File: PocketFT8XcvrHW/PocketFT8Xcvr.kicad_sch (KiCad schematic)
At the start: 56 parts, among them J1 HX8357D SPI, J2 22-23-2021, J3 GPS, J5 HX8357D 8-BIT, Q1 2N3904, Q2 2N3906, Q3 2N7000, Q4 2N7000, U1 MCP3422A1T-E/SN, U2 Si4735-D60-GU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

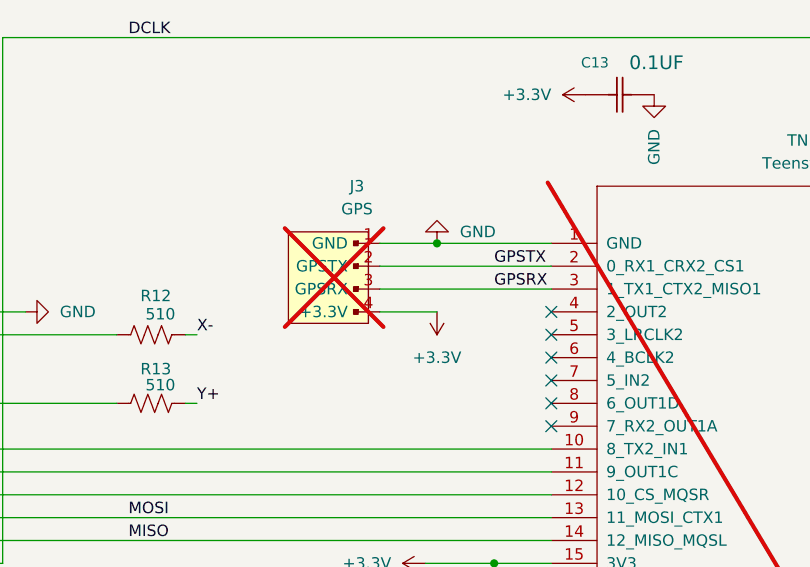
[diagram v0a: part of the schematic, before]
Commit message: Revise GPS Connector
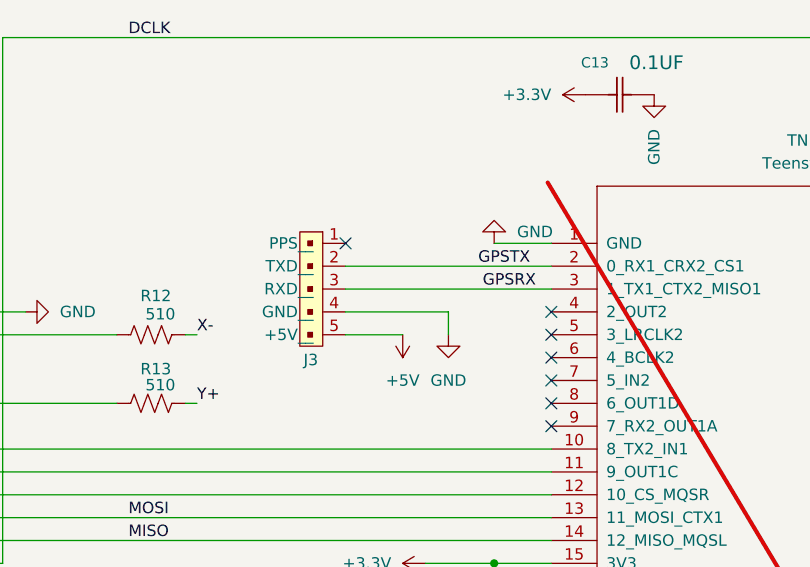
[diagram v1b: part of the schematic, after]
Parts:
- removed J3: GPS, digikey-footprints:PinHeader_1x4_P2.54mm_Drill1.02mm, symbol dk_Rectangular-Connectors-Headers-Male-Pins:0022232041
- added J3: B5B-XH-A_LF__SN_, digikey-footprints:PinHeader_1x5_P2.5mm_Drill1.1mm, symbol dk_Rectangular-Connectors-Headers-Male-Pins:B5B-XH-A_LF__SN_
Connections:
- net +5V: now also J3.5 (+5V__)
- net GND: now also J3.4 (GND__)
- net GPSRX: now also J3.3 (RXD__)
- net GPSTX: now also J3.2 (TXD__)
- no-connect marks 83 -> 84

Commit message: DRC Cleanup
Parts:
- added C18: 0.1UF, Capacitor_SMD:C_0603_1608Metric, symbol Kemet2024-08-02_22-05-35:C0603C104K4RACTU
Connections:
- net +5V: now also C18.1
- net GND: now also C18.2

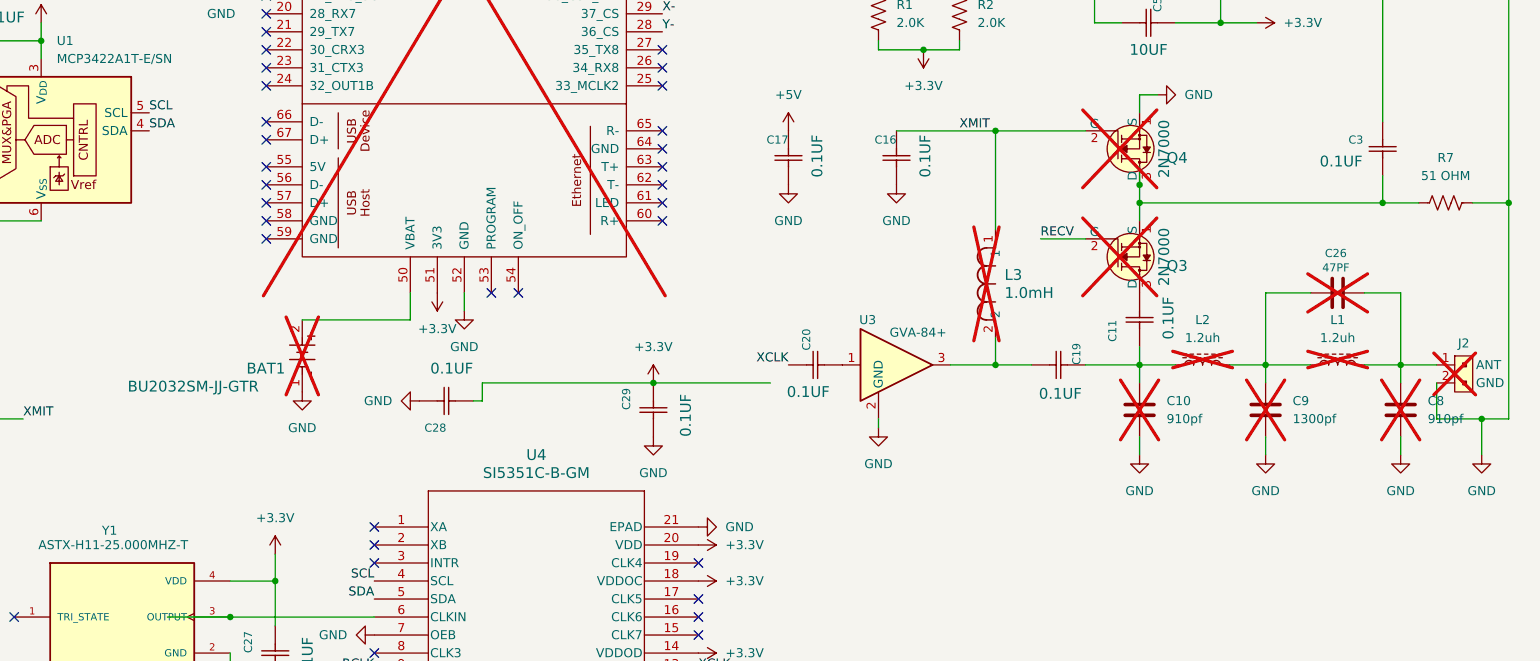
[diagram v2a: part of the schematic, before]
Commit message: Pivot to 74ACT244DWR Power Amplifier (in progress)
ToDo:  LPF values, bifilar transformer specs, QA checks (esp. XMIT/RECV logic)
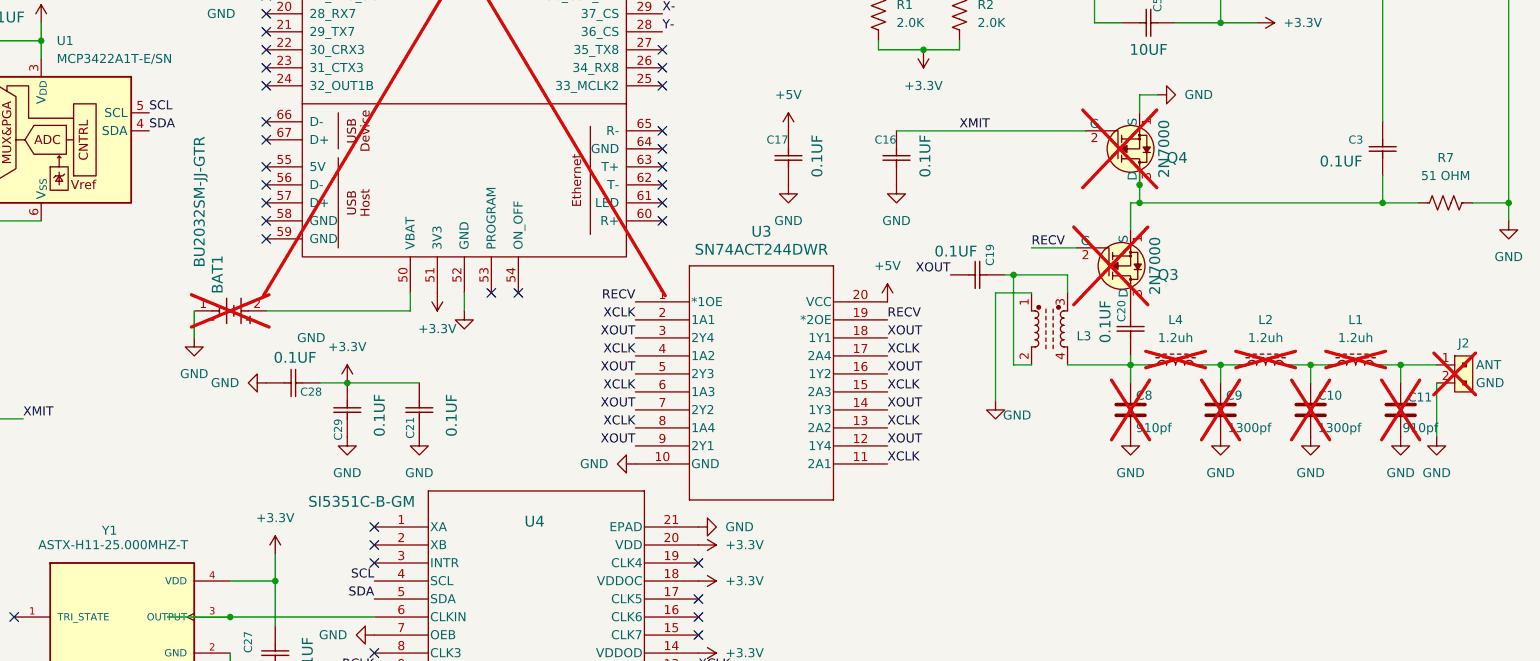
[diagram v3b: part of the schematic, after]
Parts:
- removed C20: 0.1UF, Capacitor_SMD:C_0603_1608Metric, symbol Kemet2024-08-02_22-05-35:C0603C104K4RACTU
- removed C26: 47PF, Capacitor_SMD:C_0805_2012Metric, symbol SparkFun-Capacitor:47pF_0603_50V_5%
- removed L3: 1.0mH, IND_BOURNS_RLB9012, symbol 2024-07-31_16-01-32:RLB9012-102KL
- removed U3: GVA-84+, Package_TO_SOT_SMD:SOT-89-3_Handsoldering, symbol RF_Amplifier:GVA-84
- added C21: 0.1UF, Capacitor_SMD:C_0603_1608Metric, symbol Kemet2024-08-02_22-05-35:C0603C104K4RACTU
- added C9: 1300pf, Capacitor_SMD:C_0805_2012Metric, symbol Device:C
- added L3: L_Ferrite_Coupled, symbol Device:L_Ferrite_Coupled
- added L4: 1.2uh, Inductor_THT:L_Toroid_Vertical_L10.0mm_W5.0mm_P5.08mm, symbol Device:L_Ferrite
- added U3: SN74ACT244DWR, DW20, symbol 2024-10-06_22-30-30:SN74ACT244DWR
- renumbered C9 to C10, C8 to C11, C11 to C20, C10 to C8
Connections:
- net +3.3V: now also C21.2
- net +5V: now also U3.20 (VCC)
- net GND: now also C21.1, C9.2, L3.1, U3.10 (GND)
- net RECV: now also U3.1 (*1OE), U3.19 (*2OE)
- net XCLK: now also U3.11 (2A1), U3.13 (2A2), U3.15 (2A3), U3.17 (2A4), U3.2 (1A1), U3.4 (1A2), U3.6 (1A3), U3.8 (1A4)
- net XOUT: now reaches C19.1
- net XOUT: now also U3.12 (1Y4), U3.14 (1Y3), U3.16 (1Y2), U3.18 (1Y1), U3.3 (2Y4), U3.5 (2Y3), U3.7 (2Y2), U3.9 (2Y1)
- net at C20.2, C8.1: now also L3.4, L4.1; no longer C19.2, L2.1
- new net: C19.2, L3.2, L3.3
- new net: C9.1, L2.1, L4.2
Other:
- moved on the sheet: BAT1, C10, C19, C20, C28, C29, C8, L1, L2, Q3

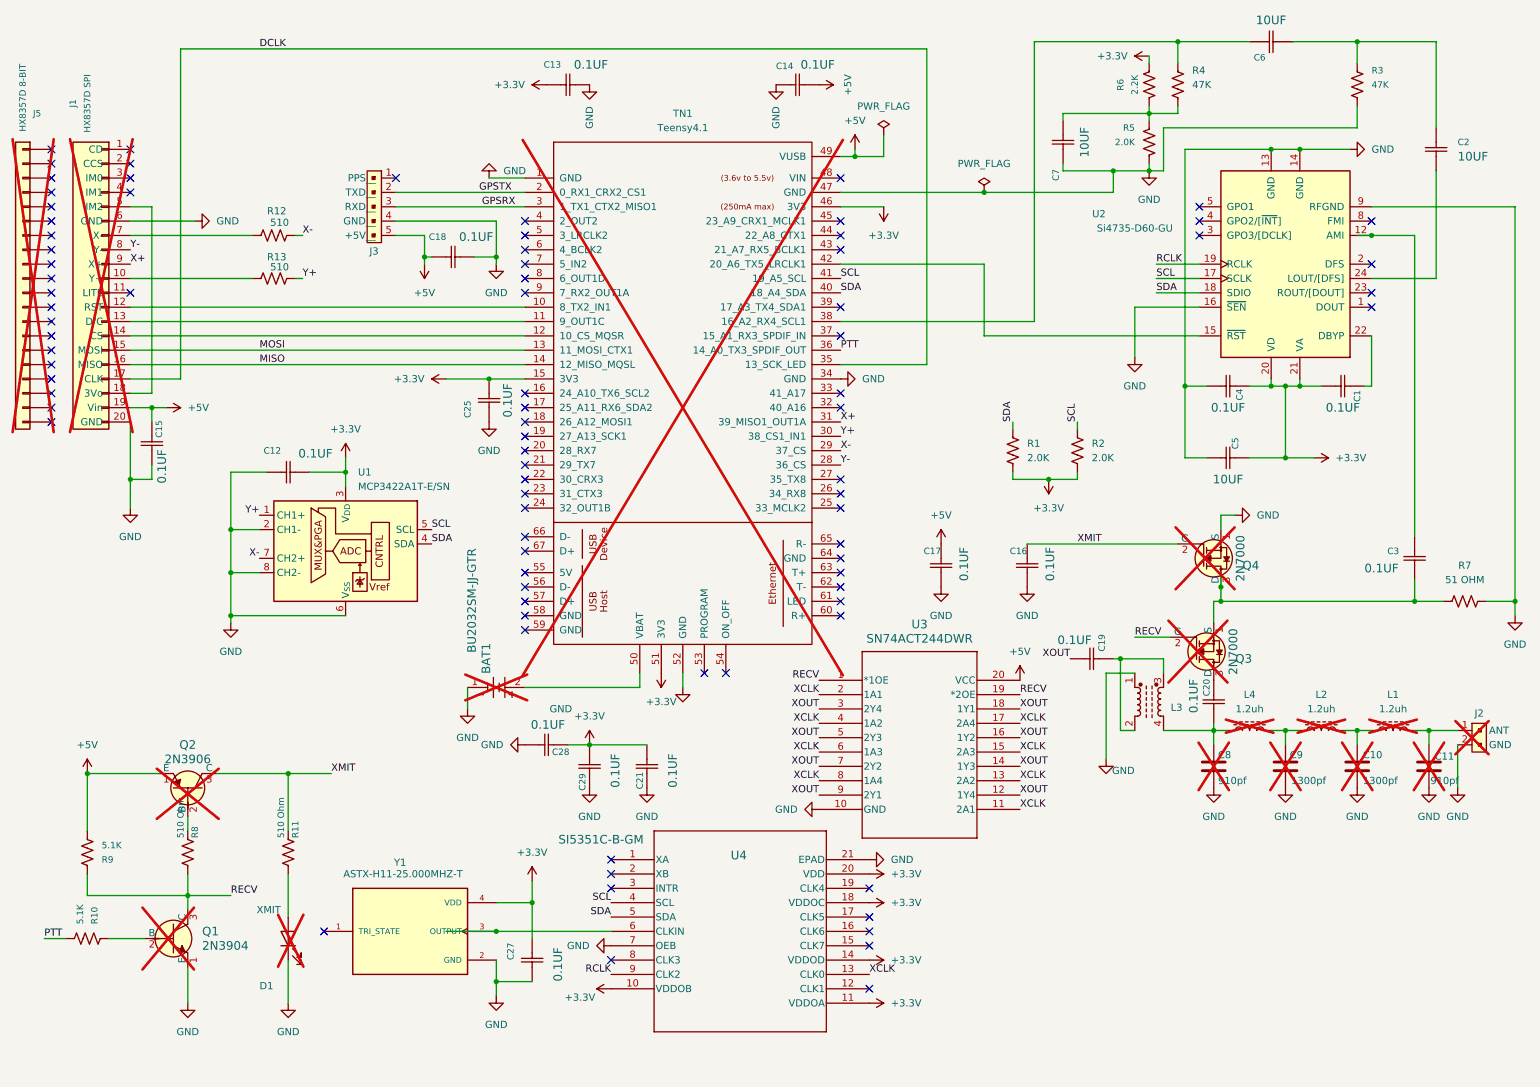
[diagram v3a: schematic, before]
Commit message: New 74ACT244 PA in progress
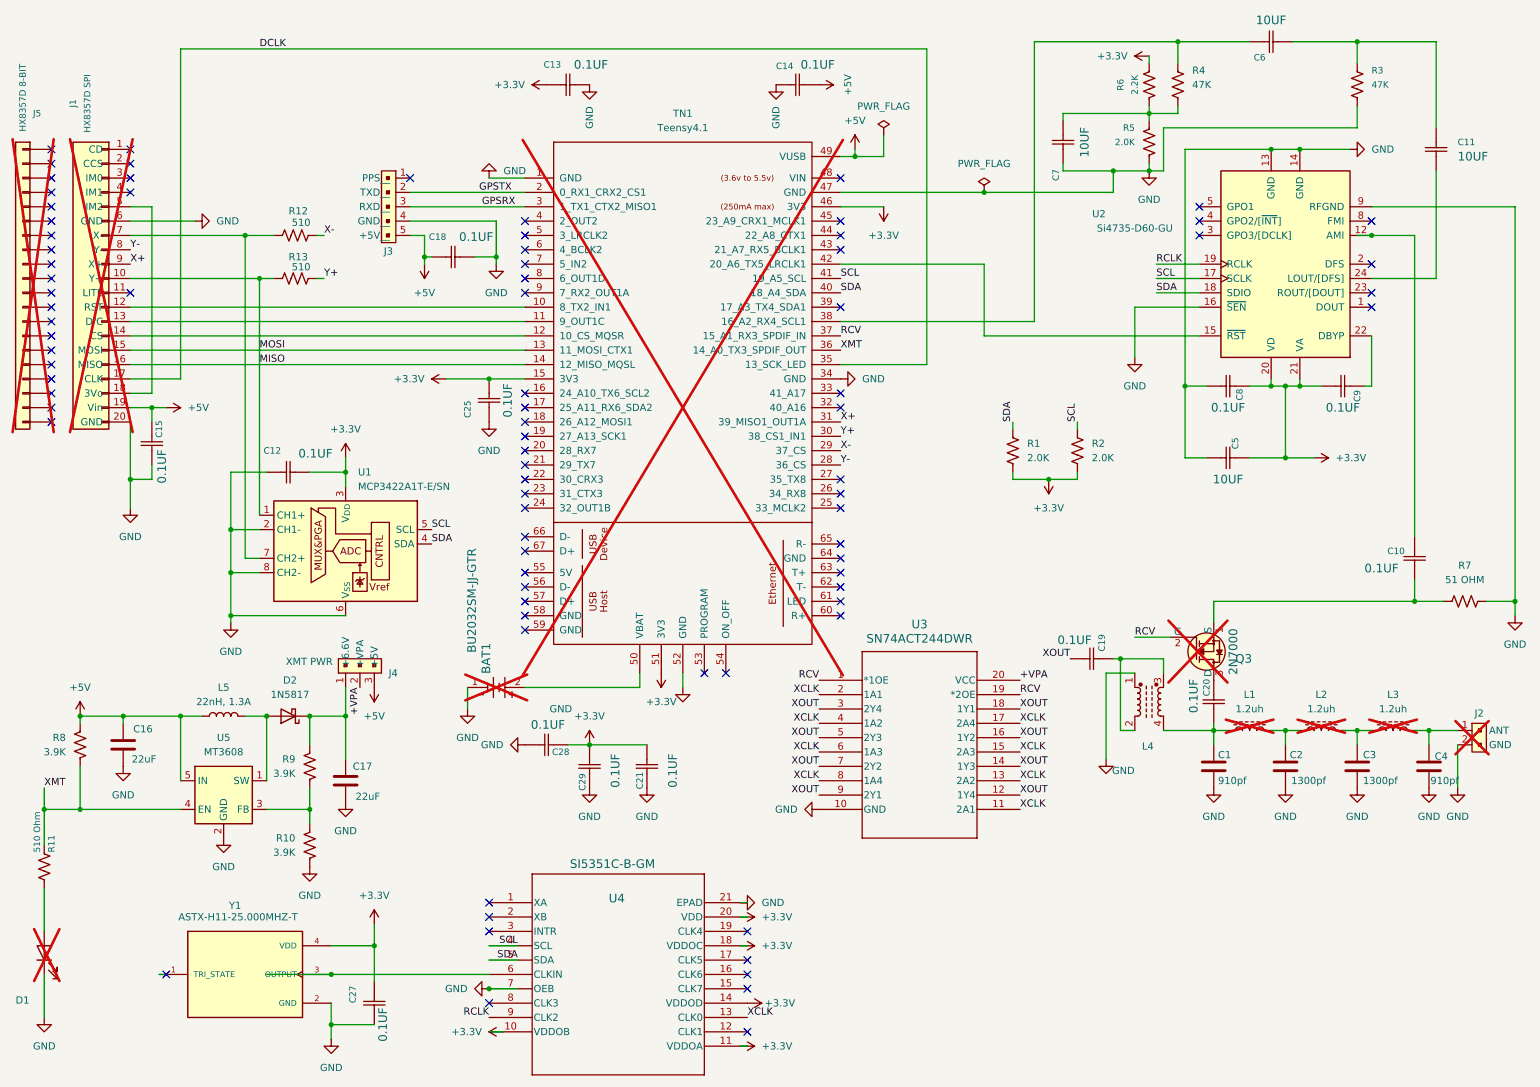
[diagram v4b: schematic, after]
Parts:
- removed C16, C17: 0.1UF, Capacitor_SMD:C_0603_1608Metric, symbol Kemet2024-08-02_22-05-35:C0603C104K4RACTU
- removed Q1: 2N3904, digikey-footprints:TO-92-3, symbol dk_Transistors-Bipolar-BJT-Single:2N3904
- removed Q2: 2N3906, digikey-footprints:TO-92-3, symbol dk_Transistors-Bipolar-BJT-Single:2N3906
- removed Q4: 2N7000, digikey-footprints:TO-92-3, symbol dk_Transistors-FETs-MOSFETs-Single:2N7000
- removed R10, R9: 5.1K, Resistor_SMD:R_0603_1608Metric, symbol SparkFun-Resistor:5.1k_0603
- removed R8: 510 Ohm, Resistor_SMD:R_0603_1608Metric, symbol Device:R_US
- added C16, C17: 22uF, 0603, symbol SparkFun-Capacitor:C
- added D2: 1N5817, 1N5817T:DO-41_DIO, symbol Device:D_Schottky
- added J4: XMT PWR, digikey-footprints:PinHeader_1x3_P2.54mm_Drill1.02mm, symbol dk_Rectangular-Connectors-Headers-Male-Pins:0022232031
- added L5: 22nH, 1.3A, 0603, symbol SparkFun-Coil:L
- added R10, R8, R9: 3.9K, Resistor_SMD:R_0603_1608Metric, symbol SparkFun-Resistor:2.0k_0603
- added U5: MT3608, Package_TO_SOT_SMD:SOT-23-6, symbol Regulator_Switching:MT3608
- C1: renamed from C8; now fitted; now in the parts list
- C2: renamed from C9; now fitted; now in the parts list
- C3: renamed from C10; now fitted; now in the parts list
- C4: renamed from C11; now fitted; now in the parts list
- L4: renamed from L3; footprint (none) -> Inductor_THT:L_Toroid_Vertical_BIFILAR
- U3: footprint DW20 -> sn74act244dwr:DW20
- renumbered C3 to C10, C2 to C11, C4 to C8, C1 to C9, L4 to L1, L1 to L3
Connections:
- net MOSI is gone; now on net MISO: J1.15 (MOSI), TN1.13 (11_MOSI_CTX1)
- net RECV is gone; now on net RCV: Q3.2 (G), U3.1 (*1OE), U3.19 (*2OE)
- net XMIT is gone; now on net XMT: R11.1
- net +5V: now also C16.1, J4.3 (+5V), L5.1, R8.1, U5.5 (IN); no longer U3.20 (VCC)
- net GND: now also C16.2, C17.2, R10.2, U5.2 (GND)
- net MISO: now also J1.10 (Y+), R13.1, U1.1 (CH1+)
- net X-: no longer U1.7 (CH2+)
- net Y+: no longer U1.1 (CH1+)
- net at J1.7 (X-), R12.1: now also U1.7 (CH2+)
- net RCV: now reaches TN1.37 (15_A1_RX3_SPDIF_IN)
- net PTT renamed XMT
- net XMT: now also R8.2, U5.4 (EN)
- new net: C17.1, D2.1 (K), J4.1 (+6.6V), R9.1
- new net: D2.2 (A), L5.2, U5.1 (SW)
- new net: R10.1, R9.2, U5.3 (FB)
- new net +VPA: J4.2 (+VPA), U3.20 (VCC)
- no-connect marks 84 -> 83
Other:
- moved on the sheet: C27, D1, J3, R11, R12, R13, U4, Y1

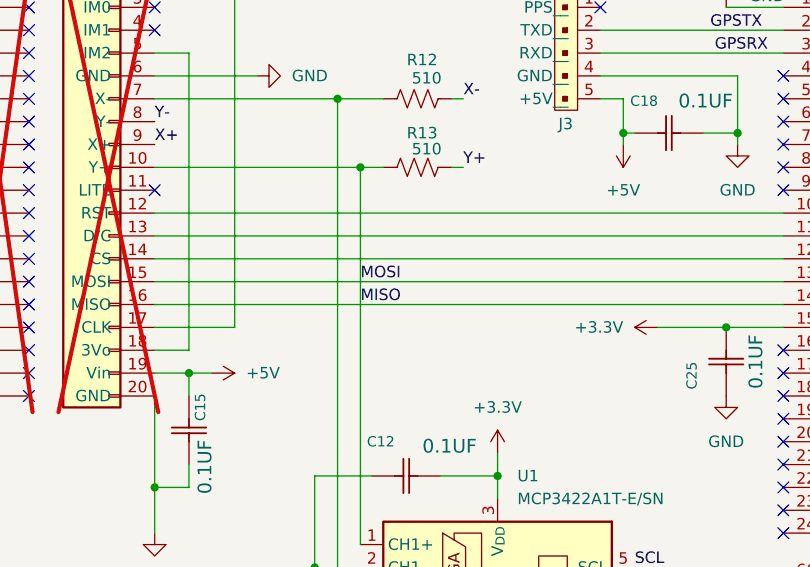
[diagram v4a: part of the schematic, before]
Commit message: Changed PA from MMIC to 74ACT244
New PA chip.
Optional step-up power supply apparently helps xmit power.
Connector for choosing PA power (5V or ~6.6V).
Misc bug fixes.
7-Pole LP filter (TODO:  Choose the real inductor/capacitor values).
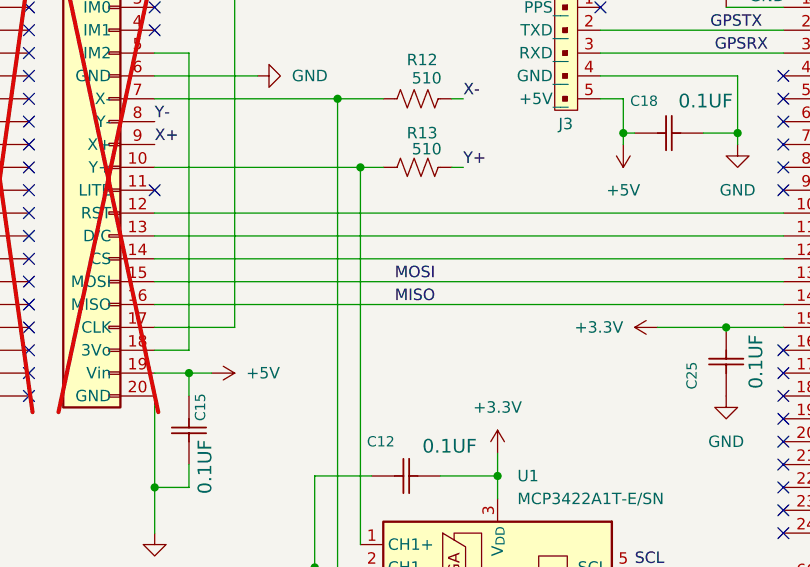
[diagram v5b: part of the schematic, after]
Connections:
- net MISO: no longer J1.10 (Y+), J1.15 (MOSI), R13.1, TN1.13 (11_MOSI_CTX1), U1.1 (CH1+)
- new net: J1.10 (Y+), R13.1, U1.1 (CH1+)
- new net MOSI: J1.15 (MOSI), TN1.13 (11_MOSI_CTX1)
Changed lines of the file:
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@@
 		)
 	)
-	(label "MOSI"
-		(at 57.15 74.93 0)
-		(fields_autoplaced yes)
-		(effects
-			(font
-				(size 1.27 1.27)
-			)
-			(justify left bottom)
-		)
-	)
 	(label "+VPA"
 		(at 74.93 134.62 270)
@@
 		)
 	)
-	(label "MISO"
-		(at 57.15 77.47 0)
-		(fields_autoplaced yes)
-		(effects
-			(font
-				(size 1.27 1.27)
-			)
-			(justify left bottom)
-		)
-	)
 	(label "XOUT"
 		(at 191.77 138.43 0)
@@
 		)
 	)
+	(label "MOSI"
+		(at 60.96 74.93 0)
+		(fields_autoplaced yes)
+		(effects
+			(font
+				(size 1.27 1.27)
+			)
+			(justify left bottom)
+		)
+	)
 	(label "XCLK"
 		(at 191.77 151.13 0)
@@
 		)
 	)
+	(label "MISO"
+		(at 60.96 77.47 0)
+		(fields_autoplaced yes)
+		(effects
+			(font
+				(size 1.27 1.27)
+			)
+			(justify left bottom)
+		)
+	)
 	(label "SCL"
 		(at 87.63 106.68 0)
@@
 			)
 		)
-		(pin "Y+"
+		(pin "2"
 		)
-		(pin "IM0"
+		(pin "14"
 		)
-		(pin "IM1"
+		(pin "15"
 		)
-		(pin "IM2"
+		(pin "4"
 		)
-		(pin "GND"
+		(pin "5"
 		)
-		(pin "X-"
+		(pin "7"
 		)
-		(pin "Y-"
+		(pin "8"
 		)
-		(pin "X+"
+		(pin "20"
 		)
-		(pin "CD"
+		(pin "3"
 		)
-		(pin "LITE"
+		(pin "12"
 		)
-		(pin "RST"
+		(pin "11"
 		)
-		(pin "D/C"
+		(pin "13"
 		)
-		(pin "CS"
+		(pin "6"
 		)
-		(pin "MOSI"
+		(pin "9"
 		)
-		(pin "MISO"
+		(pin "18"
 		)
-		(pin "CLK"
+		(pin "19"
 		)
-		(pin "3VO"
+		(pin "16"
 		)
-		(pin "+5V"
+		(pin "17"
 		)
-		(pin "CCS"
+		(pin "10"
 		)
-		(pin "GND"
+		(pin "1"
 		)
 		(instances

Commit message: Filter experiments
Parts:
- C1, C4: value 910pf -> 750 pF
- C2, C3: value 1300pf -> 1200 pF
- L1, L3: value 1.2uh -> 1.3 uH
- L2: value 1.2uh -> 1.5 uH
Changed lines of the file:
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@@
 			)
 		)
-		(property "Value" "910pf"
+		(property "Value" "750 pF"
 			(at 264.414 151.13 0)
 			(effects
@@
 			)
 		)
-		(property "Value" "1.2uh"
+		(property "Value" "1.3 uH"
 			(at 257.81 138.43 90)
 			(effects
@@
 			)
 		)
-		(property "Value" "1.2uh"
+		(property "Value" "1.5 uH"
 			(at 245.11 138.43 90)
 			(effects
@@
 			)
 		)
-		(property "Value" "1300pf"
+		(property "Value" "1200 pF"
 			(at 239.776 151.13 0)
 			(effects
@@
 			)
 		)
-		(property "Value" "1300pf"
+		(property "Value" "1200 pF"
 			(at 252.476 151.13 0)
 			(effects
@@
 			)
 		)
-		(property "Value" "1.2uh"
+		(property "Value" "1.3 uH"
 			(at 232.41 138.43 90)
 			(effects
@@
 			)
 		)
-		(property "Value" "910pf"
+		(property "Value" "750 pF"
 			(at 226.822 151.13 0)
 			(effects
